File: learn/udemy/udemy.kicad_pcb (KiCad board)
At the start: 2 copper layers, 49.4 x 28.1 mm, 13 parts, among them J1 Screw_Terminal_01x02, J2 Screw_Terminal_01x02, J3 Screw_Terminal_01x02, U1 L7809, U2 L7805

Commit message: 12/01/23 incisione vie
Settaggio dei parametri per tracciare le vie di collegamento.
Utilizzo dello strumento: calcolatrice.
Inizio tracciatura vie (blu, quindi del retro del PCB)
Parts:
- moved R2 8.21 mm to (140.3, 79.3), turned to 180 degrees
- moved J2 7.83 mm to (149.8, 60.1)
- moved J3 2.90 mm to (161.2, 60.1)
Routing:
- net GND: track 0.00 -> 110.7 mm
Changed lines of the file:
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@@
   )
   (setup
+    (stackup
+      (layer "F.SilkS" (type "Top Silk Screen"))
+      (layer "F.Paste" (type "Top Solder Paste"))
+      (layer "F.Mask" (type "Top Solder Mask") (thickness 0.01))
+      (layer "F.Cu" (type "copper") (thickness 0.035))
+      (layer "dielectric 1" (type "core") (thickness 1.51) (material "FR4") (epsilon_r 4.5) (loss_tangent 0.02))
+      (layer "B.Cu" (type "copper") (thickness 0.035))
+      (layer "B.Mask" (type "Bottom Solder Mask") (thickness 0.01))
+      (layer "B.Paste" (type "Bottom Solder Paste"))
+      (layer "B.SilkS" (type "Bottom Silk Screen"))
+      (copper_finish "None")
+      (dielectric_constraints no)
+    )
     (pad_to_mask_clearance 0)
     (pcbplotparams
@@
   )
   (footprint "TerminalBlock_Phoenix:TerminalBlock_Phoenix_MKDS-1,5-2-5.08_1x02_P5.08mm_Horizontal" (layer "F.Cu")
-    (at 158.295 59.945 180)
+    (at 161.195 60.07 180)
     (descr "Terminal Block Phoenix MKDS-1,5-2-5.08, 2 pins, pitch 5.08mm, size 10.2x9.8mm^2, drill diamater 1.3mm, pad diameter 2.6mm, see http://www.farnell.com/datasheets/100425.pdf, script-generated using https://github.com/pointhi/kicad-footprint-generator/scripts/TerminalBlock_Phoenix")
     (tags "THT Terminal Block Phoenix MKDS-1,5-2-5.08 pitch 5.08mm size 10.2x9.8mm^2 drill 1.3mm pad 2.6mm")
@@
   )
   (footprint "Resistor_THT:R_Axial_DIN0207_L6.3mm_D2.5mm_P7.62mm_Horizontal" (layer "F.Cu")
-    (at 132.14 79.175)
+    (at 140.35 79.3 180)
     (descr "Resistor, Axial_DIN0207 series, Axial, Horizontal, pin pitch=7.62mm, 0.25W = 1/4W, length*diameter=6.3*2.5mm^2, http://cdn-reichelt.de/documents/datenblatt/B400/1_4W%23YAG.pdf")
     (tags "Resistor Axial_DIN0207 series Axial Horizontal pin pitch 7.62mm 0.25W = 1/4W length 6.3mm diameter 2.5mm")
@@
     (fp_line (start 7.62 0) (end 6.96 0) (layer "F.Fab") (width 0.1))
     (fp_line (start 6.96 1.25) (end 6.96 -1.25) (layer "F.Fab") (width 0.1))
-    (pad "1" thru_hole circle (at 0 0) (size 1.6 1.6) (drill 0.8) (layers *.Cu *.Mask)
+    (pad "1" thru_hole circle (at 0 0 180) (size 1.6 1.6) (drill 0.8) (layers *.Cu *.Mask)
       (net 5 "Net-(D1-Pad1)") (pintype "passive"))
-    (pad "2" thru_hole oval (at 7.62 0) (size 1.6 1.6) (drill 0.8) (layers *.Cu *.Mask)
+    (pad "2" thru_hole oval (at 7.62 0 180) (size 1.6 1.6) (drill 0.8) (layers *.Cu *.Mask)
       (net 2 "GND") (pintype "passive"))
     (model "${KICAD6_3DMODEL_DIR}/Resistor_THT.3dshapes/R_Axial_DIN0207_L6.3mm_D2.5mm_P7.62mm_Horizontal.wrl"
@@
   )
   (footprint "TerminalBlock_Phoenix:TerminalBlock_Phoenix_MKDS-1,5-2-5.08_1x02_P5.08mm_Horizontal" (layer "F.Cu")
-    (at 141.945 59.945 180)
+    (at 149.775 60.1 180)
     (descr "Terminal Block Phoenix MKDS-1,5-2-5.08, 2 pins, pitch 5.08mm, size 10.2x9.8mm^2, drill diamater 1.3mm, pad diameter 2.6mm, see http://www.farnell.com/datasheets/100425.pdf, script-generated using https://github.com/pointhi/kicad-footprint-generator/scripts/TerminalBlock_Phoenix")
     (tags "THT Terminal Block Phoenix MKDS-1,5-2-5.08 pitch 5.08mm size 10.2x9.8mm^2 drill 1.3mm pad 2.6mm")
@@
   (gr_arc (start 116.175888 56.199873) (mid 116.6 55.185551) (end 117.619886 54.775) (layer "Edge.Cuts") (width 0.1))
   (gr_line (start 165.624112 81.400127) (end 165.624873 56.218998) (layer "Edge.Cuts") (width 0.1))
+  (segment (start 156.115 72.46) (end 156.75 73.095) (width 0.25) (layer "F.Cu") (net 2))
+  (segment (start 123.61 72.475) (end 123.61 62.615) (width 0.25) (layer "B.Cu") (net 2))
+  (segment (start 123.61 72.865) (end 117.6 78.875) (width 0.25) (layer "B.Cu") (net 2))
+  (segment (start 146.555 81.3) (end 134.125 81.3) (width 0.25) (layer "B.Cu") (net 2))
+  (segment (start 132.73 79.3) (end 128.775 79.3) (width 0.25) (layer "B.Cu") (net 2))
+  (segment (start 154.075 80.1) (end 149.455 80.1) (width 0.25) (layer "B.Cu") (net 2))
+  (segment (start 156.115 60.07) (end 156.115 72.46) (width 0.25) (layer "B.Cu") (net 2))
+  (segment (start 149.455 80.1) (end 148.605 79.25) (width 0.25) (layer "B.Cu") (net 2))
+  (segment (start 143.225 61.57) (end 144.695 60.1) (width 0.25) (layer "B.Cu") (net 2))
+  (segment (start 156.75 73.095) (end 156.75 77.425) (width 0.25) (layer "B.Cu") (net 2))
+  (segment (start 123.61 62.615) (end 120.94 59.945) (width 0.25) (layer "B.Cu") (net 2))
+  (segment (start 122.565 61.57) (end 143.225 61.57) (width 0.25) (layer "B.Cu") (net 2))
+  (segment (start 156.75 77.425) (end 155.2 78.975) (width 0.25) (layer "B.Cu") (net 2))
+  (segment (start 134.125 81.3) (end 134.125 80.695) (width 0.25) (layer "B.Cu") (net 2))
+  (segment (start 134.125 80.695) (end 132.73 79.3) (width 0.25) (layer "B.Cu") (net 2))
+  (segment (start 120.94 59.945) (end 122.565 61.57) (width 0.25) (layer "B.Cu") (net 2))
+  (segment (start 128.775 79.3) (end 128.7 79.225) (width 0.25) (layer "B.Cu") (net 2))
+  (segment (start 155.55 79.325) (end 155.2 78.975) (width 0.25) (layer "B.Cu") (net 2))
+  (segment (start 159.225 79.325) (end 155.55 79.325) (width 0.25) (layer "B.Cu") (net 2))
+  (segment (start 128.7 77.565) (end 123.61 72.475) (width 0.25) (layer "B.Cu") (net 2))
+  (segment (start 155.2 78.975) (end 154.075 80.1) (width 0.25) (layer "B.Cu") (net 2))
+  (segment (start 128.7 79.225) (end 128.7 77.565) (width 0.25) (layer "B.Cu") (net 2))
+  (segment (start 156.115 72.46) (end 156.75 73.095) (width 0.25) (layer "B.Cu") (net 2))
+  (segment (start 123.61 72.475) (end 123.61 72.865) (width 0.25) (layer "B.Cu") (net 2))
+  (segment (start 148.605 79.25) (end 146.555 81.3) (width 0.25) (layer "B.Cu") (net 2))
 )

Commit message: 13/01/2023 continuazione col collegamento del e PCB
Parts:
- moved D1 2.02 mm to (137.7, 72.0), turned to 180 degrees
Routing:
- net +12V: track 0.00 -> 70.0 mm
- net /9v out: track 0.00 -> 38.4 mm, vias 0 -> 2
- net /5v out: track 0.00 -> 33.6 mm
- net Net-(D1-Pad1): track 0.00 -> 8.38 mm
- net Net-(D2-Pad1): track 0.00 -> 7.51 mm
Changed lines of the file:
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@@
   )
   (footprint "LED_THT:LED_D4.0mm" (layer "F.Cu")
-    (at 135.675 72.325)
+    (at 137.675 72.025 180)
     (descr "LED, diameter 4.0mm, 2 pins, http://www.kingbright.com/attachments/file/psearch/000/00/00/L-43GD(Ver.12B).pdf")
     (tags "LED diameter 4.0mm 2 pins")
@@
     (fp_arc (start -0.73 -1.32665) (mid 3.67 0.000306) (end -0.730339 1.32614) (layer "F.Fab") (width 0.1))
     (fp_circle (center 1.27 0) (end 3.27 0) (layer "F.Fab") (width 0.1) (fill none))
-    (pad "1" thru_hole rect (at 0 0) (size 1.8 1.8) (drill 0.9) (layers *.Cu *.Mask)
+    (pad "1" thru_hole rect (at 0 0 180) (size 1.8 1.8) (drill 0.9) (layers *.Cu *.Mask)
       (net 5 "Net-(D1-Pad1)") (pinfunction "K") (pintype "passive"))
-    (pad "2" thru_hole circle (at 2.54 0) (size 1.8 1.8) (drill 0.9) (layers *.Cu *.Mask)
+    (pad "2" thru_hole circle (at 2.54 0 180) (size 1.8 1.8) (drill 0.9) (layers *.Cu *.Mask)
       (net 3 "/9v out") (pinfunction "A") (pintype "passive"))
     (model "${KICAD6_3DMODEL_DIR}/LED_THT.3dshapes/LED_D4.0mm.wrl"
@@
   (gr_arc (start 116.175888 56.199873) (mid 116.6 55.185551) (end 117.619886 54.775) (layer "Edge.Cuts") (width 0.1))
   (gr_line (start 165.624112 81.400127) (end 165.624873 56.218998) (layer "Edge.Cuts") (width 0.1))
+  (segment (start 157.240991 75.75) (end 162.975 75.75) (width 0.25) (layer "F.Cu") (net 1))
+  (segment (start 121.07 76.595) (end 123.7 79.225) (width 0.25) (layer "F.Cu") (net 1))
+  (segment (start 127.8 61.725) (end 142.84 61.725) (width 0.25) (layer "F.Cu") (net 1))
+  (segment (start 126.02 59.945) (end 127.8 61.725) (width 0.25) (layer "F.Cu") (net 1))
+  (segment (start 154.585991 73.095) (end 157.240991 75.75) (width 0.25) (layer "F.Cu") (net 1))
+  (segment (start 126.02 59.945) (end 126.02 67.525) (width 0.25) (layer "F.Cu") (net 1))
+  (segment (start 126.02 67.525) (end 121.07 72.475) (width 0.25) (layer "F.Cu") (net 1))
+  (segment (start 121.07 72.475) (end 121.07 76.595) (width 0.25) (layer "F.Cu") (net 1))
+  (segment (start 164.225 77) (end 164.225 79.325) (width 0.25) (layer "F.Cu") (net 1))
+  (segment (start 142.84 61.725) (end 154.21 73.095) (width 0.25) (layer "F.Cu") (net 1))
+  (segment (start 162.975 75.75) (end 164.225 77) (width 0.25) (layer "F.Cu") (net 1))
+  (segment (start 154.21 73.095) (end 154.585991 73.095) (width 0.25) (layer "F.Cu") (net 1))
   (segment (start 156.115 72.46) (end 156.75 73.095) (width 0.25) (layer "F.Cu") (net 2))
   (segment (start 123.61 72.475) (end 123.61 62.615) (width 0.25) (layer "B.Cu") (net 2))
@@
   (segment (start 123.61 72.475) (end 123.61 72.865) (width 0.25) (layer "B.Cu") (net 2))
   (segment (start 148.605 79.25) (end 146.555 81.3) (width 0.25) (layer "B.Cu") (net 2))
+  (segment (start 135.135 72.025) (end 126.6 72.025) (width 0.25) (layer "F.Cu") (net 3))
+  (segment (start 135.135 72.025) (end 140.885 66.275) (width 0.25) (layer "F.Cu") (net 3))
+  (segment (start 125.175 75.15) (end 125.175 73.45) (width 0.8) (layer "F.Cu") (net 3))
+  (segment (start 126.6 72.025) (end 126.15 72.475) (width 0.25) (layer "F.Cu") (net 3))
+  (segment (start 140.885 66.275) (end 143.6 66.275) (width 0.25) (layer "F.Cu") (net 3))
+  (segment (start 125.175 73.45) (end 126.15 72.475) (width 0.8) (layer "F.Cu") (net 3))
+  (via (at 143.6 66.275) (size 0.8) (drill 0.4) (layers "F.Cu" "B.Cu") (net 3))
+  (via (at 125.175 75.15) (size 0.8) (drill 0.4) (layers "F.Cu" "B.Cu") (net 3))
+  (segment (start 121.45 78.875) (end 125.175 75.15) (width 0.8) (layer "B.Cu") (net 3))
+  (segment (start 143.6 66.275) (end 149.775 60.1) (width 0.25) (layer "B.Cu") (net 3))
+  (segment (start 120.1 78.875) (end 121.45 78.875) (width 0.8) (layer "B.Cu") (net 3))
+  (segment (start 165.482292 79.658699) (end 164.565991 80.575) (width 0.25) (layer "F.Cu") (net 4))
+  (segment (start 154.3 80.575) (end 152.7 78.975) (width 0.25) (layer "F.Cu") (net 4))
+  (segment (start 165.482292 77.207292) (end 165.482292 79.658699) (width 0.25) (layer "F.Cu") (net 4))
+  (segment (start 164.565991 80.575) (end 154.3 80.575) (width 0.25) (layer "F.Cu") (net 4))
+  (segment (start 146.69 72.965) (end 146.69 72) (width 0.25) (layer "F.Cu") (net 4))
+  (segment (start 159.29 73.095) (end 161.37 73.095) (width 0.25) (layer "F.Cu") (net 4))
+  (segment (start 152.7 78.975) (end 146.69 72.965) (width 0.25) (layer "F.Cu") (net 4))
+  (segment (start 161.37 73.095) (end 165.482292 77.207292) (width 0.25) (layer "F.Cu") (net 4))
+  (segment (start 140.35 79.3) (end 140.35 74.7) (width 0.25) (layer "F.Cu") (net 5))
+  (segment (start 140.35 74.7) (end 137.675 72.025) (width 0.25) (layer "F.Cu") (net 5))
+  (segment (start 144.15 78.625) (end 143.525 79.25) (width 0.25) (layer "F.Cu") (net 6))
+  (segment (start 144.15 72) (end 144.15 78.625) (width 0.25) (layer "F.Cu") (net 6))
 )

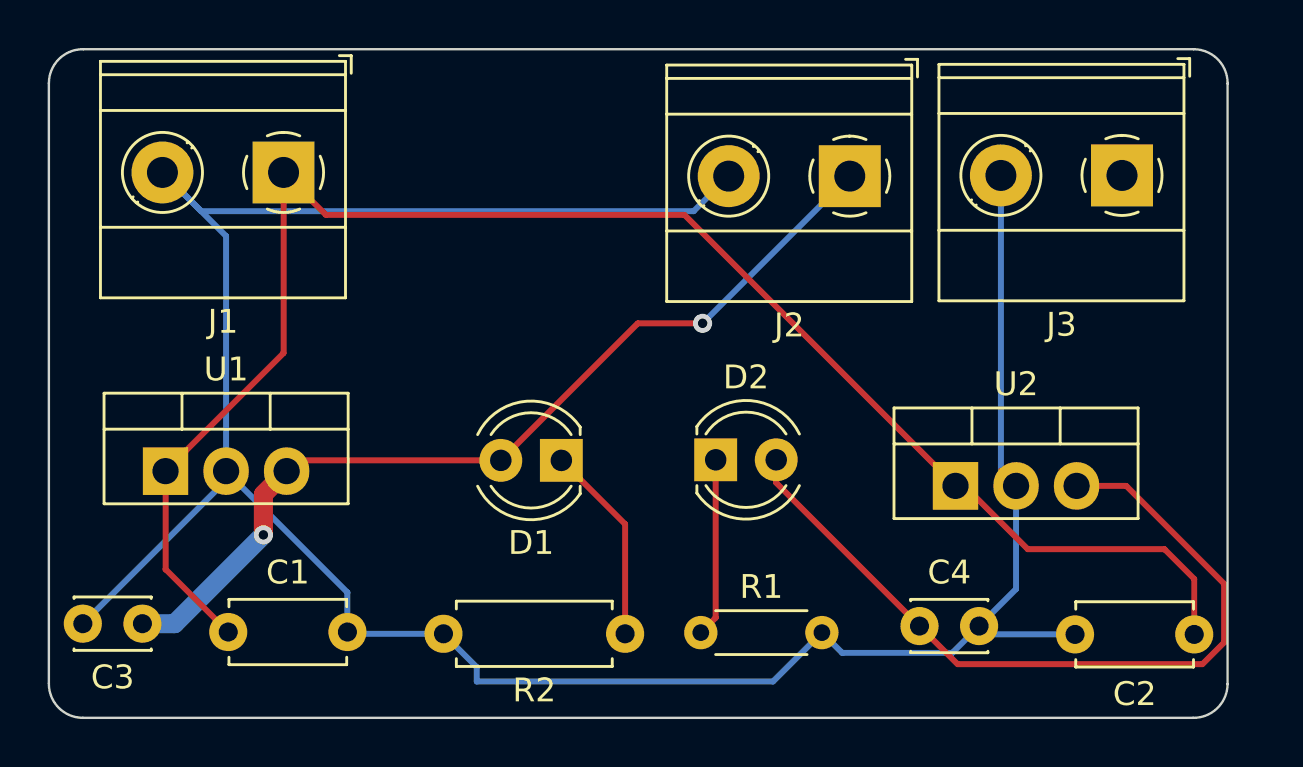
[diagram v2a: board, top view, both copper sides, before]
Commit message: 15/01/23 correzione pcb tracce
Bisogna aumentare la portata delle tracce
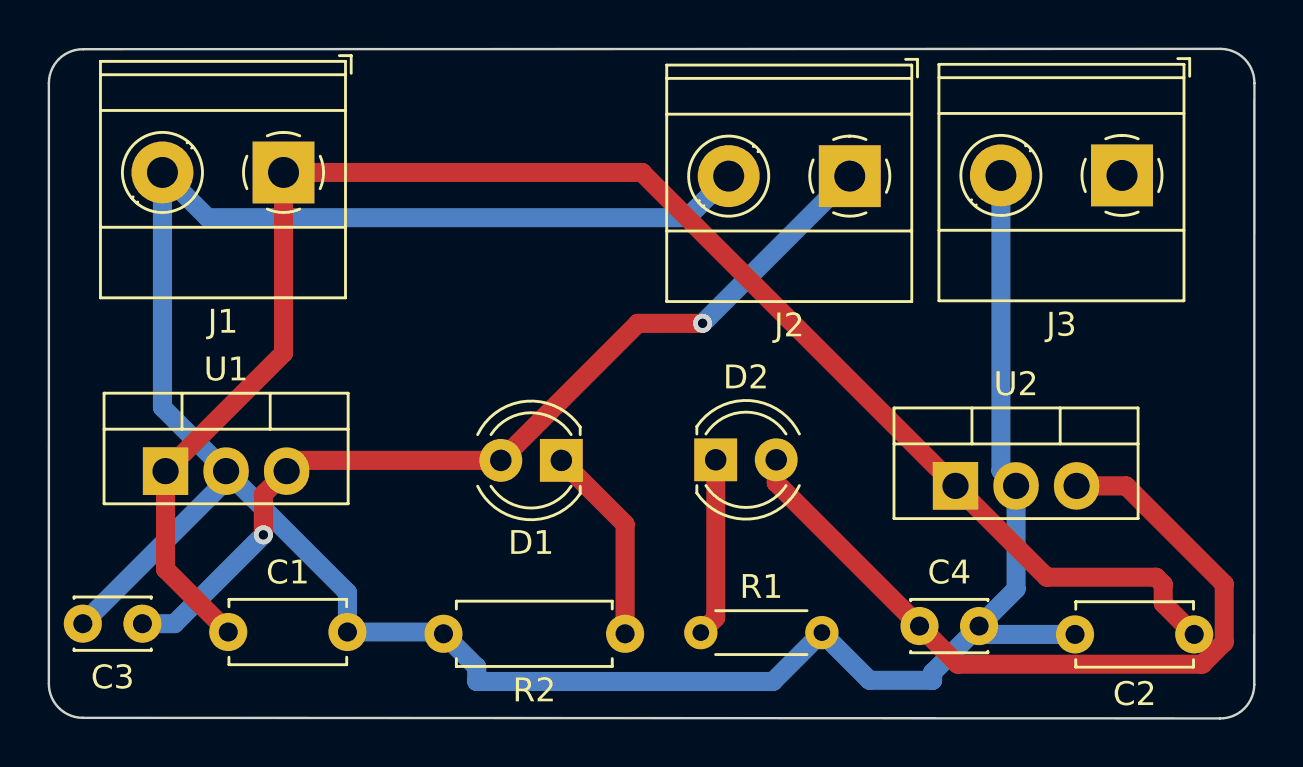
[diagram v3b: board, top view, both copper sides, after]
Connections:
- C1 pad 1: +12V -> GND
- C2 pad 1: +12V -> GND
- C3 pad 1: /9v out -> GND
- C4 pad 1: /5v out -> GND
- D1 pad 2: /9v out -> GND
- D2 pad 2: /5v out -> GND
- J1 pad 1: +12V -> GND
- J2 pad 1: /9v out -> GND
- U1 pad 1: +12V -> GND
- U1 pad 3: /9v out -> GND
- U2 pad 1: +12V -> GND
- U2 pad 3: /5v out -> GND
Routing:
- net GND: track 110.7 -> 255.1 mm, vias 0 -> 2
- net +12V: track 70.0 -> 0.00 mm
- net /9v out: track 38.4 -> 0.00 mm, vias 2 -> 0
- net /5v out: track 33.6 -> 0.00 mm
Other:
- board size 49.4 x 28.1 mm -> 50.6 x 28.1 mm

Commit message: 18/01/23 correzione PCB
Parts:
- moved R1 8.05 mm to (151.5, 77.9)
- moved C4 6.57 mm to (146.2, 78.0)
- moved U2 2.89 mm to (151.7, 71.7)
- moved D2 2.30 mm to (142.1, 71.0), turned to 180 degrees
- moved D1 2.04 mm to (135.9, 71.1)
- moved C3 1.93 mm to (121.7, 77.8)
- moved C1 1.61 mm to (125.0, 78.3)
- moved C2 1.58 mm to (164.1, 77.8)
- moved J2 1.37 mm to (151.1, 60.0)
- moved R2 1.37 mm to (141.3, 78.3)
- moved J3 1.28 mm to (162.5, 60.0)
- moved U1 0.97 mm to (120.4, 71.8)
- moved J1 0.27 mm to (126.3, 60.0)
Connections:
- C1 pad 1: GND -> +12V
- C2 pad 1: GND -> +12V
- C3 pad 1: GND -> /9v out
- C4 pad 1: GND -> /5v out
- D1 pad 2: GND -> /9v out
- D2 pad 2: GND -> /5v out
- J1 pad 1: GND -> +12V
- J2 pad 1: GND -> /9v out
- U1 pad 1: GND -> +12V
- U1 pad 3: GND -> /9v out
- U2 pad 1: GND -> +12V
- U2 pad 3: GND -> /5v out
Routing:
- net GND: track 255.1 -> 108.4 mm, vias 2 -> 0
- net +12V: track 0.00 -> 67.8 mm
- net /5v out: track 0.00 -> 56.6 mm
- net /9v out: track 0.00 -> 38.5 mm, vias 0 -> 2
- net Net-(D2-Pad1): track 7.51 -> 12.2 mm
- net Net-(D1-Pad1): track 8.38 -> 9.50 mm
- added copper zone on F.Cu, net (none)

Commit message: 22/01/23 aggiunto testo nel retro del PCB
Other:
- board text added: "Regolatore di tensione da 5 a 9 volt."
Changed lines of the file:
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@@
   (gr_arc (start 116.175888 56.199873) (mid 116.6 55.185551) (end 117.619886 54.775) (layer "Edge.Cuts") (width 0.1))
   (gr_line (start 166.743998 81.425127) (end 166.749873 56.204549) (layer "Edge.Cuts") (width 0.1))
+  (gr_text "Regolatore di tensione da 5 a 9 volt." (at 143.575 63.375) (layer "B.SilkS")
+    (effects (font (size 1.5 1.5) (thickness 0.3)) (justify mirror))
+  )
   (segment (start 149.875 79.2) (end 148.7 78.025) (width 0.8) (layer "B.Cu") (net 1))
   (segment (start 135.646418 80.281418) (end 146.443582 80.281418) (width 0.8) (layer "B.Cu") (net 1))
